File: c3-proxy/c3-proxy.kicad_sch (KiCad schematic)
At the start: 19 parts, among them J1 TFM-120-X1-XXX-D-RA, J2 SFM-120-02-L-DH, J3 USB_C_Receptacle_USB2.0_16P, J4 Barrel_Jack_Switch_MountingPin, J5 Conn_01x04, U9 IP4234CZ6,125

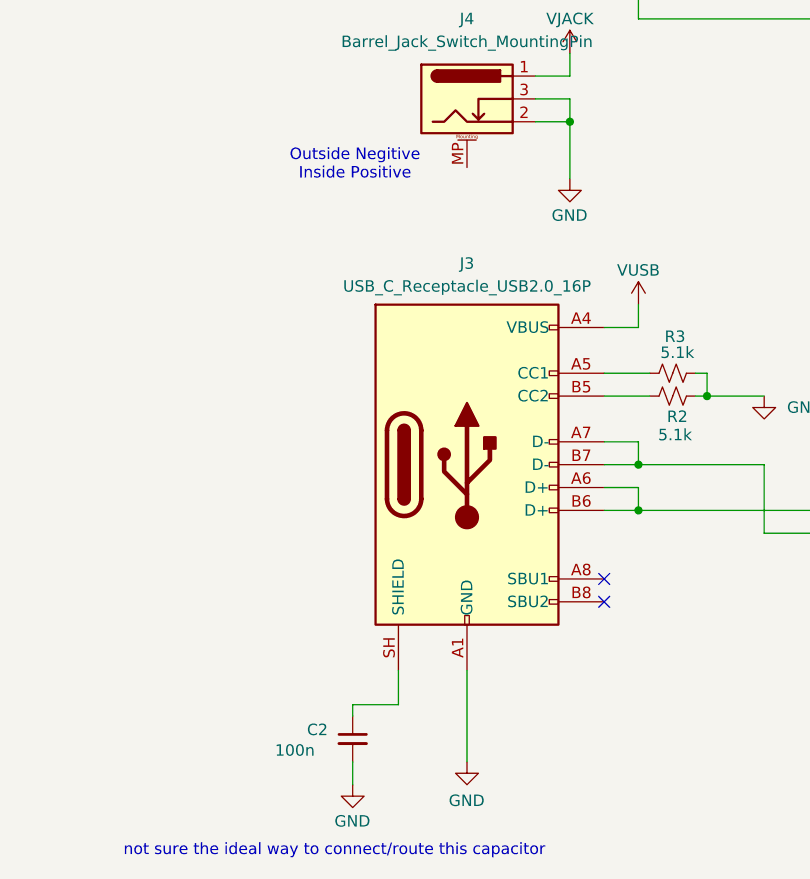
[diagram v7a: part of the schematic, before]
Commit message: changed footprints in schematic
so that "update from schematic" doesn't kill my baby resistors
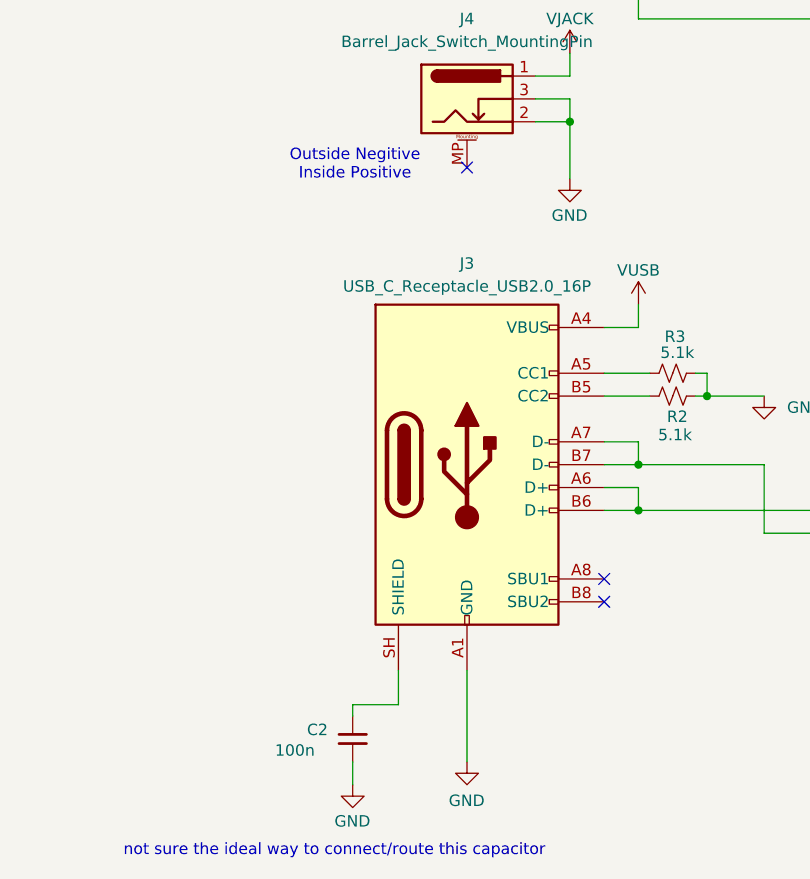
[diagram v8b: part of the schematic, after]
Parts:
- C2: footprint oresat-passives:0603-A -> oresat-passives:0603-C-NOSILK; DIST DigiKey -> (none); DPN 399-6856-1-ND -> (none); MFR KEMET -> (none); MPN C0603C104K5RACAUTO -> (none)
- R2, R3: footprint oresat-passives:0603-A -> oresat-passives:0603-C-NOSILK
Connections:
- no-connect marks 2 -> 3
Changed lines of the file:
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@@
 	)
 	(no_connect
+		(at 109.22 170.18)
+	)
+	(no_connect
 		(at 124.46 218.44)
 	)
@@
 			)
 		)
-		(property "Footprint" "oresat-passives:0603-A"
+		(property "Footprint" "oresat-passives:0603-C-NOSILK"
 			(at 132.08 193.04 0)
 			(hide yes)
@@
 			)
 		)
-		(property "Footprint" "oresat-passives:0603-A"
+		(property "Footprint" "oresat-passives:0603-C-NOSILK"
 			(at 132.08 195.58 0)
 			(hide yes)
@@
 			)
 		)
-		(property "Footprint" "oresat-passives:0603-A"
-			(at 96.52 233.68 0)
-			(hide yes)
-			(show_name no)
-			(do_not_autoplace no)
-			(effects
-				(font
-					(size 1.27 1.27)
-				)
-			)
-		)
-		(property "Datasheet" "https://search.kemet.com/download/specsheet/C0603C104K5RACAUTO"
+		(property "Footprint" "oresat-passives:0603-C-NOSILK"
 			(at 96.52 233.68 0)
 			(hide yes)
@@
 			)
 		)
-		(property "Description" "0.1 µF ±10% 50V Ceramic Capacitor X7R 0603 (1608 Metric)"
-			(at 96.52 233.68 0)
-			(hide yes)
-			(show_name no)
-			(do_not_autoplace no)
-			(effects
-				(font
-					(size 1.27 1.27)
-				)
-			)
-		)
-		(property "DIST" "DigiKey"
-			(at 96.52 233.68 0)
-			(hide yes)
-			(show_name no)
-			(do_not_autoplace no)
-			(effects
-				(font
-					(size 1.27 1.27)
-				)
-			)
-		)
-		(property "DPN" "399-6856-1-ND"
-			(at 96.52 233.68 0)
-			(hide yes)
-			(show_name no)
-			(do_not_autoplace no)
-			(effects
-				(font
-					(size 1.27 1.27)
-				)
-			)
-		)
-		(property "MFR" "KEMET"
+		(property "Datasheet" ""
 			(at 96.52 233.68 0)
 			(hide yes)
@@
 			)
 		)
-		(property "MPN" "C0603C104K5RACAUTO"
-			(at 96.52 233.68 0)
+		(property "Description" "Unpolarized capacitor, small symbol"
+			(at 96.52 243.84 0)
 			(hide yes)
 			(show_name no)
